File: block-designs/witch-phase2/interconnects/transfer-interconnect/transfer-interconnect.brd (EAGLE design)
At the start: 142.2 x 71.1 mm, 14 parts

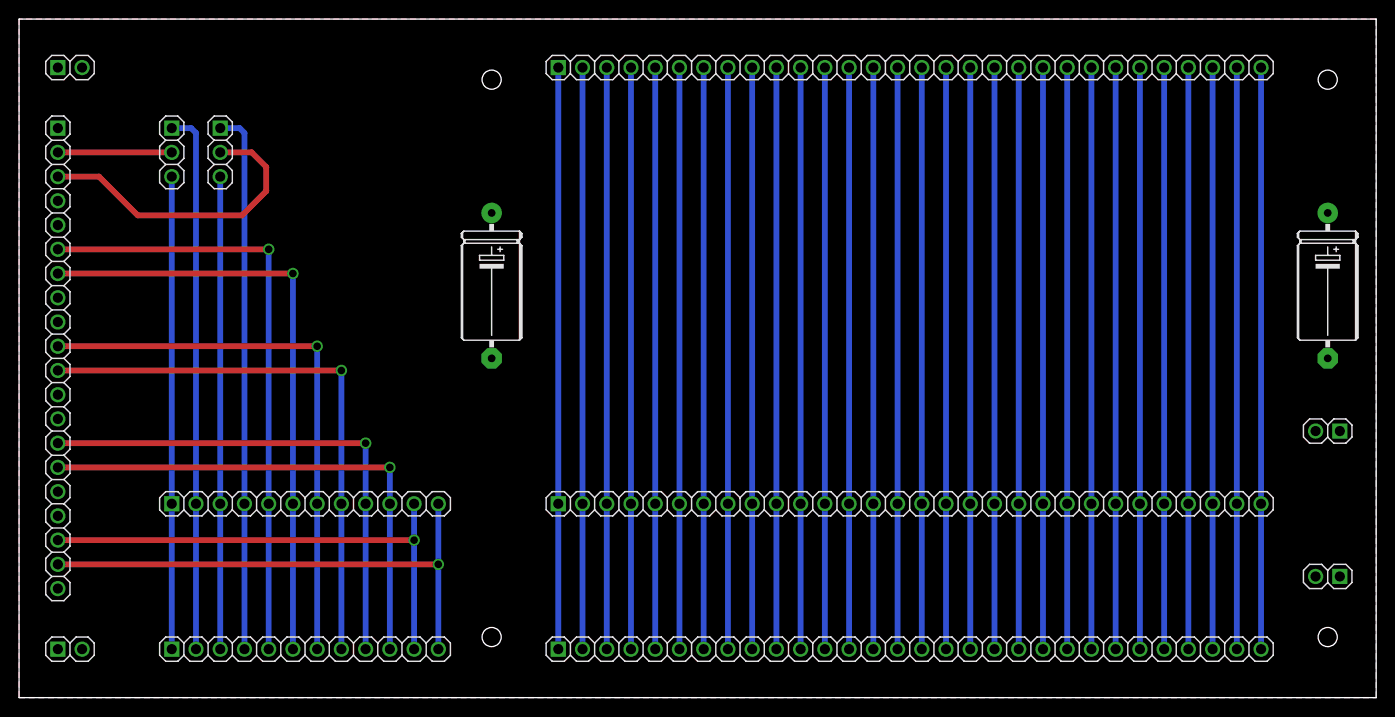
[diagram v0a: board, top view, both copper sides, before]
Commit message: fixes for layout and connections
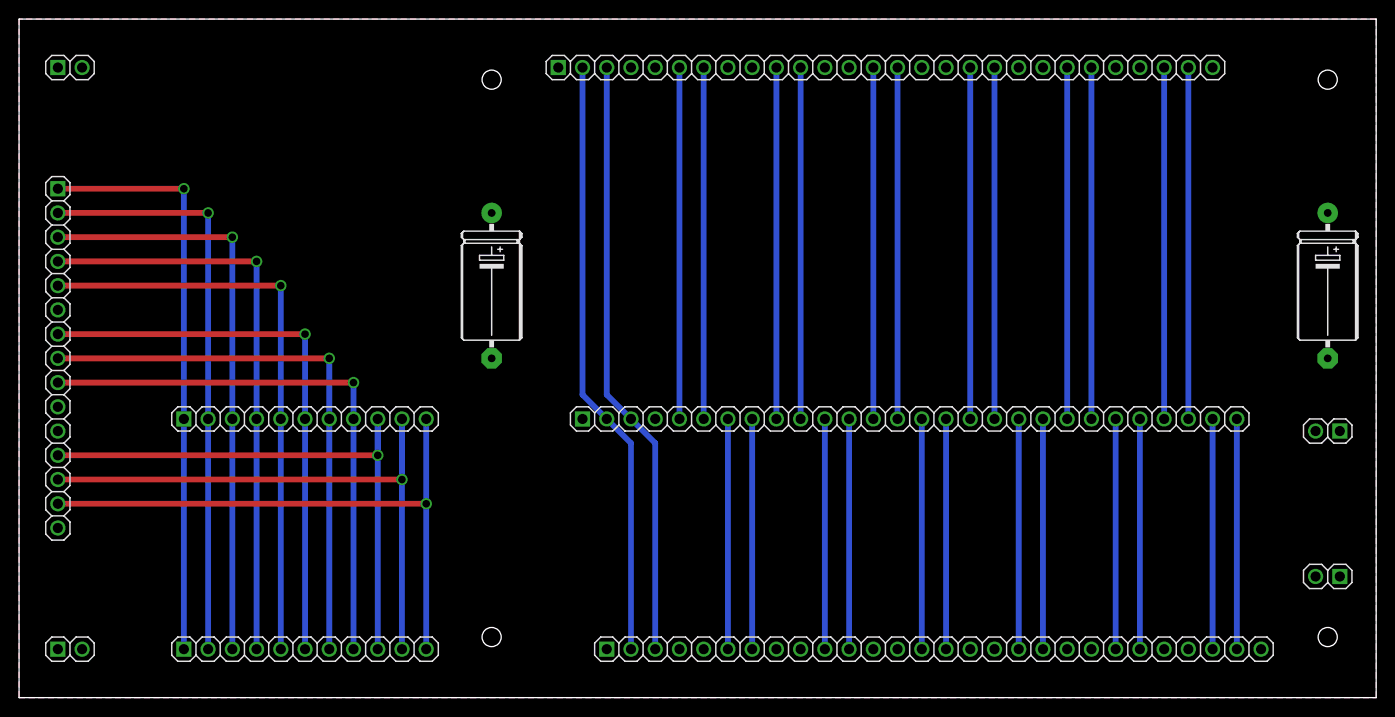
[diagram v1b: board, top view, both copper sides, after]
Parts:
- removed JP1: (no value), pinhead:1X20
- removed JP10, JP3: (no value), pinhead:1X03
- added JP13: (no value), pinhead:1X15
- JP2, JP9: device pinhead:1X12 -> pinhead:1X11
- JP4, JP5, JP6: device pinhead:1X30 -> pinhead:1X28
- moved JP6 8.89 mm to (93.3, 29.2)
- moved JP9 8.89 mm to (30.0, 29.2)
- moved JP5 2.54 mm to (95.9, 5.08)
- moved JP4 2.54 mm to (90.8, 66.0)
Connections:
- removed net N$1 (its old number): JP4.30, JP5.30, JP6.30
- removed net N$2 (its old number): JP4.29, JP5.29, JP6.29
- removed net N$27: JP4.4, JP5.4, JP6.4
- removed net N$30: JP4.1, JP5.1, JP6.1
- removed net N$31: JP1.19, JP2.12, JP9.12
- removed net N$43: JP1.3, JP3.2
- removed net N$44: JP1.2, JP10.2
- net GND: now also JP13.11, JP13.6, JP4.1, JP4.13, JP4.17, JP4.21, JP4.25, JP4.5, JP4.9, JP5.1, JP5.13, JP5.17, JP5.21, JP5.25, JP5.5, JP5.9; no longer JP1.13, JP1.17, JP1.4, JP1.5, JP1.9
- net N$10: now also JP4.19, JP6.18; no longer JP4.21, JP5.21, JP6.21
- net N$11: now also JP4.22, JP6.21; no longer JP4.20, JP5.20, JP6.20
- net N$12: now also JP4.23, JP6.22; no longer JP4.19, JP5.19, JP6.19
- net N$13: now also JP4.26, JP6.25; no longer JP4.18, JP5.18, JP6.18
- net N$14: now also JP4.27, JP6.26; no longer JP4.17, JP5.17, JP6.17
- net N$15: now also JP5.6, JP6.7; no longer JP4.16, JP5.16, JP6.16
- net N$16: now also JP5.7, JP6.8; no longer JP4.15, JP5.15, JP6.15
- net N$17: now also JP5.10, JP6.11; no longer JP4.14, JP5.14, JP6.14
- net N$18: now also JP5.11, JP6.12; no longer JP4.13, JP5.13, JP6.13
- net N$19: now also JP5.14, JP6.15; no longer JP4.12, JP5.12, JP6.12
- net N$20: now also JP5.15, JP6.16; no longer JP4.11, JP5.11, JP6.11
- net N$21: now also JP5.18, JP6.19; no longer JP4.10, JP5.10, JP6.10
- net N$22: now also JP5.19, JP6.20; no longer JP4.9, JP5.9, JP6.9
- net N$23: now also JP5.22, JP6.23; no longer JP4.8, JP5.8, JP6.8
- net N$24: now also JP5.23, JP6.24; no longer JP4.7, JP5.7, JP6.7
- net N$25: now also JP5.26, JP6.27; no longer JP4.6, JP5.6, JP6.6
- net N$26: now also JP5.27, JP6.28; no longer JP4.5, JP5.5, JP6.5
- net N$3: now also JP4.10, JP6.9; no longer JP4.28, JP5.28, JP6.28
- net N$32: now also JP13.14; no longer JP1.18
- net N$33: now also JP13.13; no longer JP1.15
- net N$34: now also JP13.12; no longer JP1.14
- net N$35: now also JP13.9; no longer JP1.11
- net N$36: now also JP13.8; no longer JP1.10
- net N$37: now also JP13.7; no longer JP1.7
- net N$38: now also JP13.5; no longer JP1.6
- net N$39: now also JP13.4; no longer JP3.1
- net N$4: now also JP4.11, JP6.10; no longer JP4.27, JP5.27, JP6.27
- net N$40: now also JP13.3; no longer JP3.3
- net N$41: now also JP13.2; no longer JP10.1
- net N$46: now also JP13.1; no longer JP10.3
- net N$5: now also JP4.6, JP6.5; no longer JP4.26, JP5.26, JP6.26
- net N$6: now also JP4.7, JP6.6; no longer JP4.25, JP5.25, JP6.25
- net N$7: now also JP4.14, JP6.13; no longer JP4.24, JP5.24, JP6.24
- net N$8: now also JP4.15, JP6.14; no longer JP4.23, JP5.23, JP6.23
- net N$9: now also JP4.18, JP6.17; no longer JP4.22, JP5.22, JP6.22
- net VCC: now also JP13.10, JP13.15, JP4.12, JP4.16, JP4.20, JP4.24, JP4.28, JP4.4, JP4.8, JP5.12, JP5.16, JP5.20, JP5.24, JP5.28, JP5.4, JP5.8; no longer JP1.1, JP1.12, JP1.16, JP1.20, JP1.8
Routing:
- net N$30: track 61.0 -> 0.00 mm
- net N$27: track 61.0 -> 0.00 mm
- net N$2 (its old number): track 61.0 -> 0.00 mm
- net N$1 (its old number): track 61.0 -> 0.00 mm
- net N$31: track 55.1 -> 0.00 mm, vias 1 -> 0
- net N$26: track 61.0 -> 24.1 mm
- net N$25: track 61.0 -> 24.1 mm
- net N$24: track 61.0 -> 24.1 mm
- net N$23: track 61.0 -> 24.1 mm
- net N$22: track 61.0 -> 24.1 mm
- net N$21: track 61.0 -> 24.1 mm
- net N$20: track 61.0 -> 24.1 mm
- net N$19: track 61.0 -> 24.1 mm
- net N$18: track 61.0 -> 24.1 mm
- net N$17: track 61.0 -> 24.1 mm
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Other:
- board text added: "Transfer Interconnect Board"
- board text removed: "Mini-Store Interconnect Board"

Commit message: add schmitt-triggers to receive signals
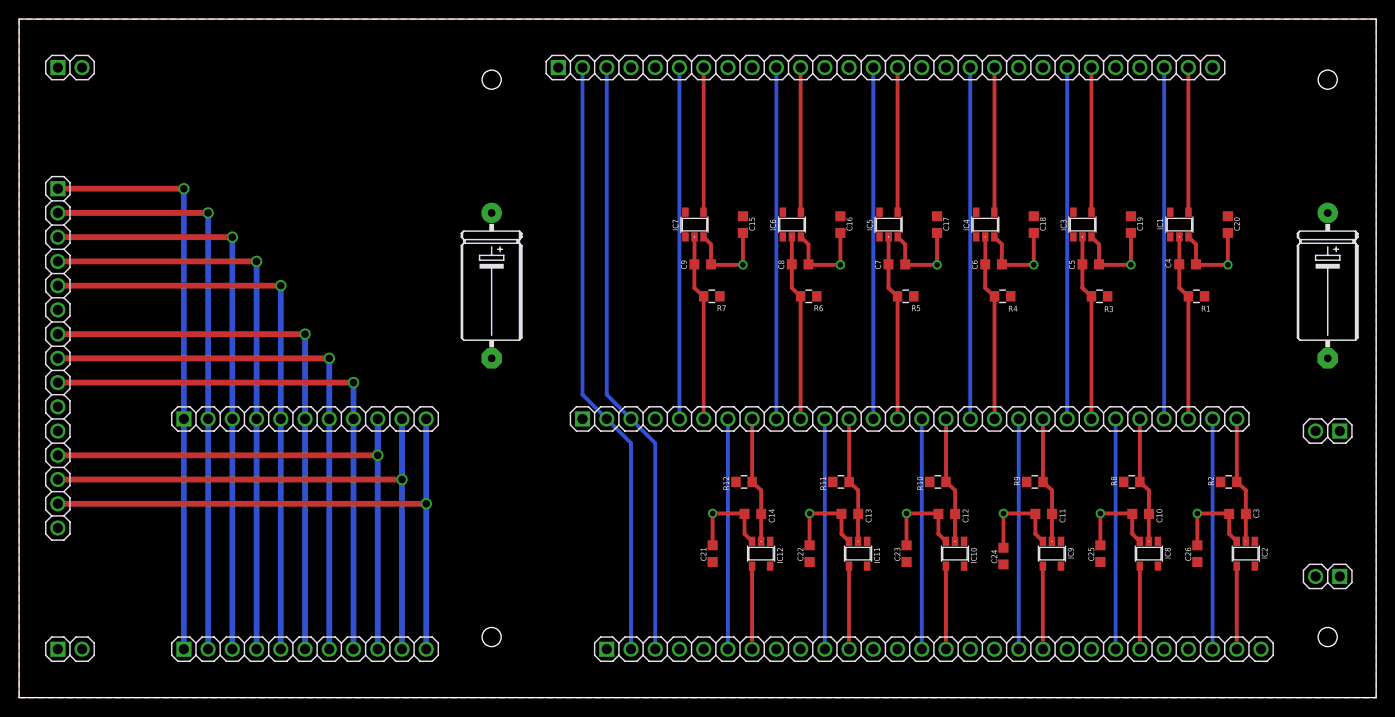
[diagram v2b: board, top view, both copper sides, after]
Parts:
- added C10, C11, C12, C13, C14, C15, C16, C17, C18, C19, C20, C21, C22, C23, C24, C25, C26, C3, C4, C5, C6, C7, C8, C9: 1uF, resistor:C0603K
- added IC1, IC10, IC11, IC12, IC2, IC3, IC4, IC5, IC6, IC7, IC8, IC9: 74LVC1G14DBV, 74xx-little-us:SOT23-5
- added R1, R10, R11, R12, R2, R3, R4, R5, R6, R7, R8, R9: 100k, resistor:R0603
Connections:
- removed net N$10: JP4.19, JP6.18
- removed net N$12: JP4.23, JP6.22
- removed net N$14: JP4.27, JP6.26
- removed net N$16: JP5.7, JP6.8
- removed net N$18: JP5.11, JP6.12
- removed net N$20: JP5.15, JP6.16
- removed net N$22: JP5.19, JP6.20
- removed net N$24: JP5.23, JP6.24
- removed net N$26: JP5.27, JP6.28
- removed net N$4: JP4.11, JP6.10
- removed net N$6: JP4.7, JP6.6
- removed net N$8: JP4.15, JP6.14
- new net IN5: C8.1, IC6.2, R6.1
- new net IN6: C9.1, IC7.2, R7.1
- new net INA1: C4.1, IC1.2, JP6.26, R1.1
- new net INA2: C5.1, IC3.2, JP6.22, R3.1
- new net INA3: C6.1, IC4.2, JP6.18, R4.1
- new net INA4: C7.1, IC5.2, JP6.14, R5.1
- new net INA5: JP6.10
- new net INA6: JP6.6
- new net INB1: C3.1, IC2.2, JP6.28, R2.1
- new net INB2: C10.1, IC8.2, JP6.24, R8.1
- new net INB3: C11.1, IC9.2, JP6.20, R9.1
- new net INB4: C12.1, IC10.2, JP6.16, R10.1
- new net INB5: C13.1, IC11.2, JP6.12, R11.1
- new net INB6: C14.1, IC12.2, JP6.8, R12.1
- new net OUTA1: IC1.4, JP4.27
- new net OUTA2: IC3.4, JP4.23
- new net OUTA3: IC4.4, JP4.19
- new net OUTA4: IC5.4, JP4.15
- new net OUTA5: IC6.4, JP4.11
- new net OUTA6: IC7.4, JP4.7
- new net OUTB1: IC2.4, JP5.27
- new net OUTB2: IC8.4, JP5.23
- new net OUTB3: IC9.4, JP5.19
- new net OUTB4: IC10.4, JP5.15
- new net OUTB5: IC11.4, JP5.11
- new net OUTB6: IC12.4, JP5.7
- net GND: now also C10.2, C11.2, C12.2, C13.2, C14.2, C15.2, C16.2, C17.2, C18.2, C19.2, C20.2, C21.2, C22.2, C23.2, C24.2, C25.2, C26.2, C3.2, C4.2, C5.2, C6.2, C7.2, C8.2, C9.2, IC1.3, IC10.3, IC11.3, IC12.3, IC2.3, IC3.3, IC4.3, IC5.3, IC6.3, IC7.3, IC8.3, IC9.3
- net VCC: now also C15.1, C16.1, C17.1, C18.1, C19.1, C20.1, C21.1, C22.1, C23.1, C24.1, C25.1, C26.1, IC1.5, IC10.5, IC11.5, IC12.5, IC2.5, IC3.5, IC4.5, IC5.5, IC6.5, IC7.5, IC8.5, IC9.5, R1.2, R10.2, R11.2, R12.2, R2.2, R3.2, R4.2, R5.2, R6.2, R7.2, R8.2, R9.2
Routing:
- net GND: track 0.00 -> 119.1 mm, vias 0 -> 12
- net N$8: track 36.8 -> 0.00 mm
- net N$6: track 36.8 -> 0.00 mm
- net N$4: track 36.8 -> 0.00 mm
- net N$14: track 36.8 -> 0.00 mm
- net N$12: track 36.8 -> 0.00 mm
- net N$10: track 36.8 -> 0.00 mm
- net N$26: track 24.1 -> 0.00 mm
- net N$24: track 24.1 -> 0.00 mm
- net N$22: track 24.1 -> 0.00 mm
- net N$20: track 24.1 -> 0.00 mm
- net N$18: track 24.1 -> 0.00 mm
- net N$16: track 24.1 -> 0.00 mm
- net INA3: track 0.00 -> 19.5 mm
- net IN6: track 0.00 -> 19.5 mm
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
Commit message: minor cleanup
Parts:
- IC1, IC10, IC11, IC12, IC2, IC3, IC4, IC5, IC6, IC7, IC8, IC9: value 74LVC1G14DBV -> 74LVC1G17DBV

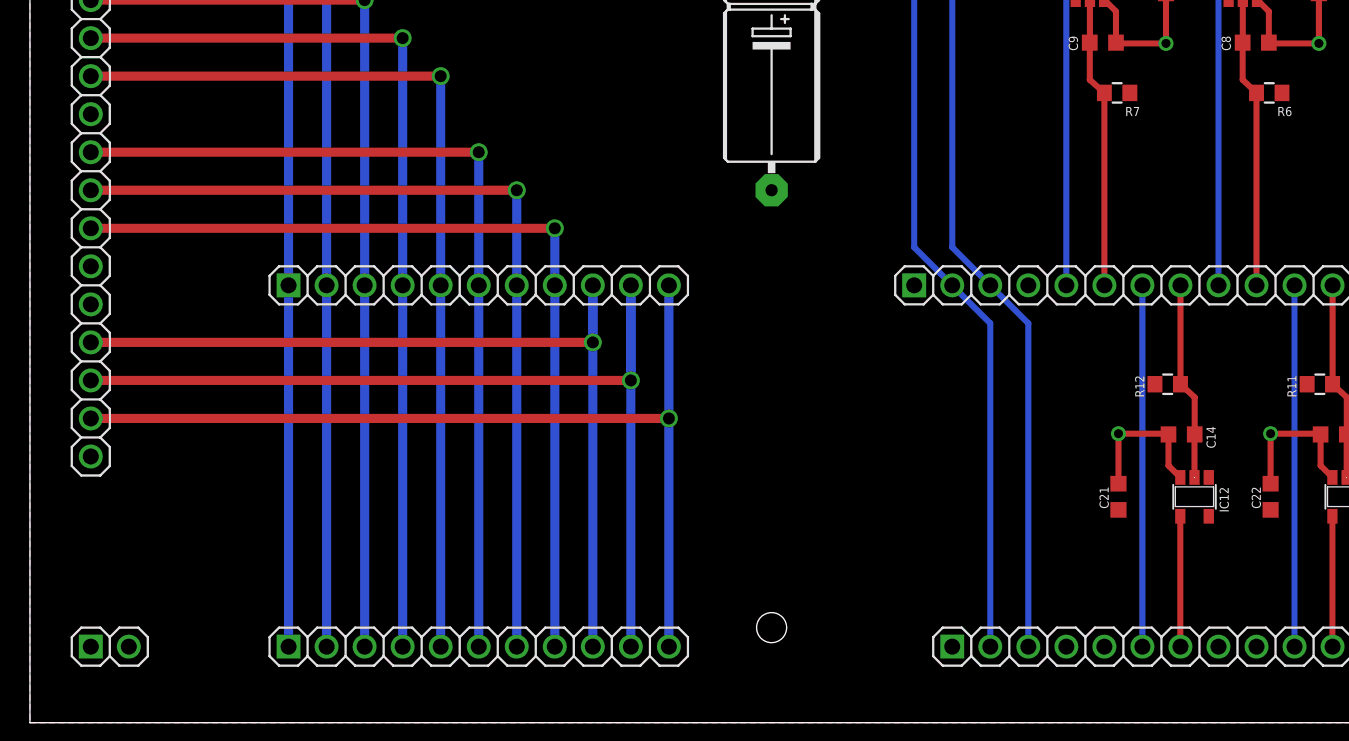
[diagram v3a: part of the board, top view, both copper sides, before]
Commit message: add schmitt trigger on the carry output line
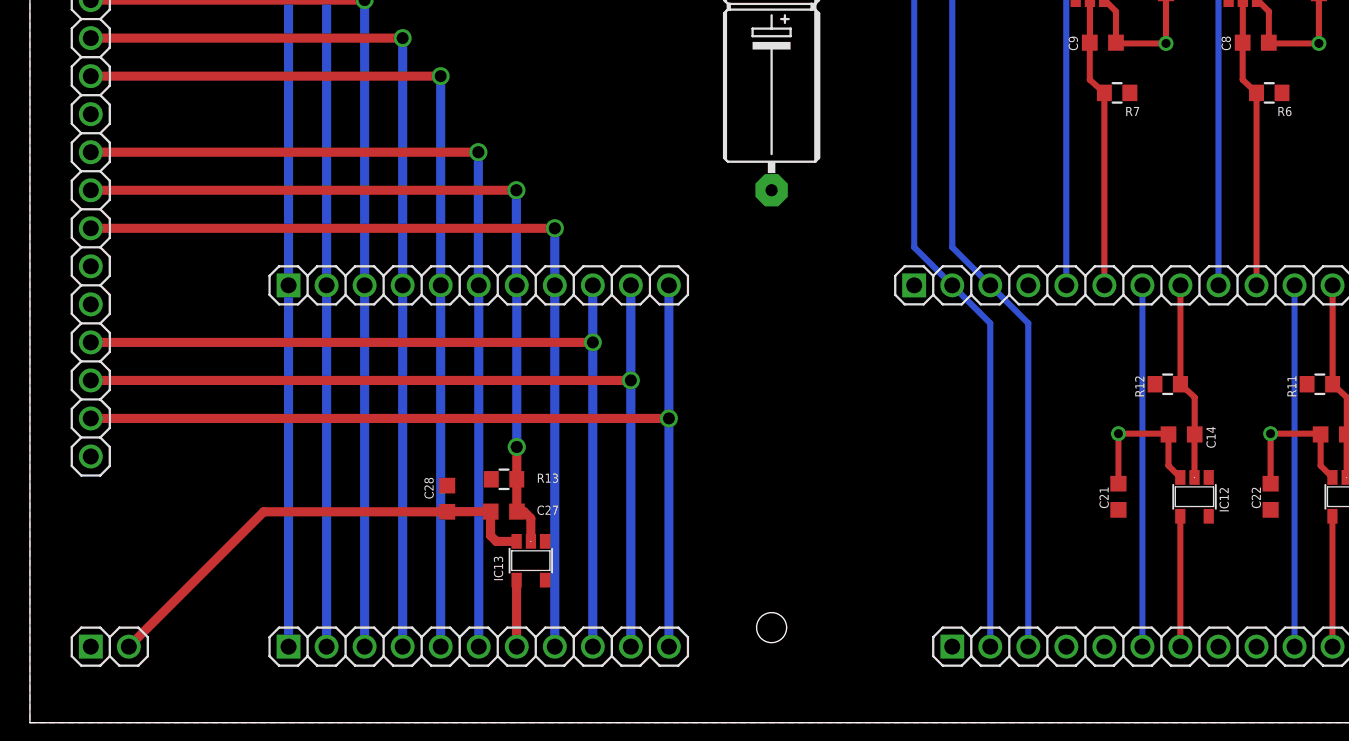
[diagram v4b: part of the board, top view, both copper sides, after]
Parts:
- added C27, C28: 1uF, resistor:C0603K
- added IC13: 74LVC1G17DBV, 74xx-little-us:SOT23-5
- added R13: 100k, resistor:R0603
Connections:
- removed net IN5: C8.1, IC6.2, R6.1
- removed net IN6: C9.1, IC7.2, R7.1
- removed net N$36: JP13.8, JP2.7, JP9.7
- new net CARRY_IN: C27.1, IC13.2, JP13.8, JP9.7, R13.1
- new net CARRY_OUT: IC13.4, JP2.7
- net GND: now also C27.2, C28.2, IC13.3
- net INA5: now also C8.1, IC6.2, R6.1
- net INA6: now also C9.1, IC7.2, R7.1
- net VCC: now also C28.1, IC13.5, R13.2
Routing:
- net N$36: track 58.9 -> 0.00 mm, vias 1 -> 0
- net CARRY_IN: track 0.00 -> 53.1 mm, vias 0 -> 2
- net GND: track 119.1 -> 150.5 mm
- net INA6: track 0.00 -> 19.5 mm
- net IN6: track 19.5 -> 0.00 mm
- net INA5: track 0.00 -> 19.5 mm
- net IN5: track 19.5 -> 0.00 mm
- net N$33: track 66.5 -> 60.2 mm
- net CARRY_OUT: track 0.00 -> 4.44 mm
- net N$34: track 61.5 -> 57.7 mm
